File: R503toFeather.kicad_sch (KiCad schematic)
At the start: 4 parts, among them J1 MX1.0 6P

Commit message: RP2350 HSTX Production Version
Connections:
- net at A1.16 (SPARE): no longer J1.2 (GND)
- net at A1.17 (SDA): now also J1.2 (GND)

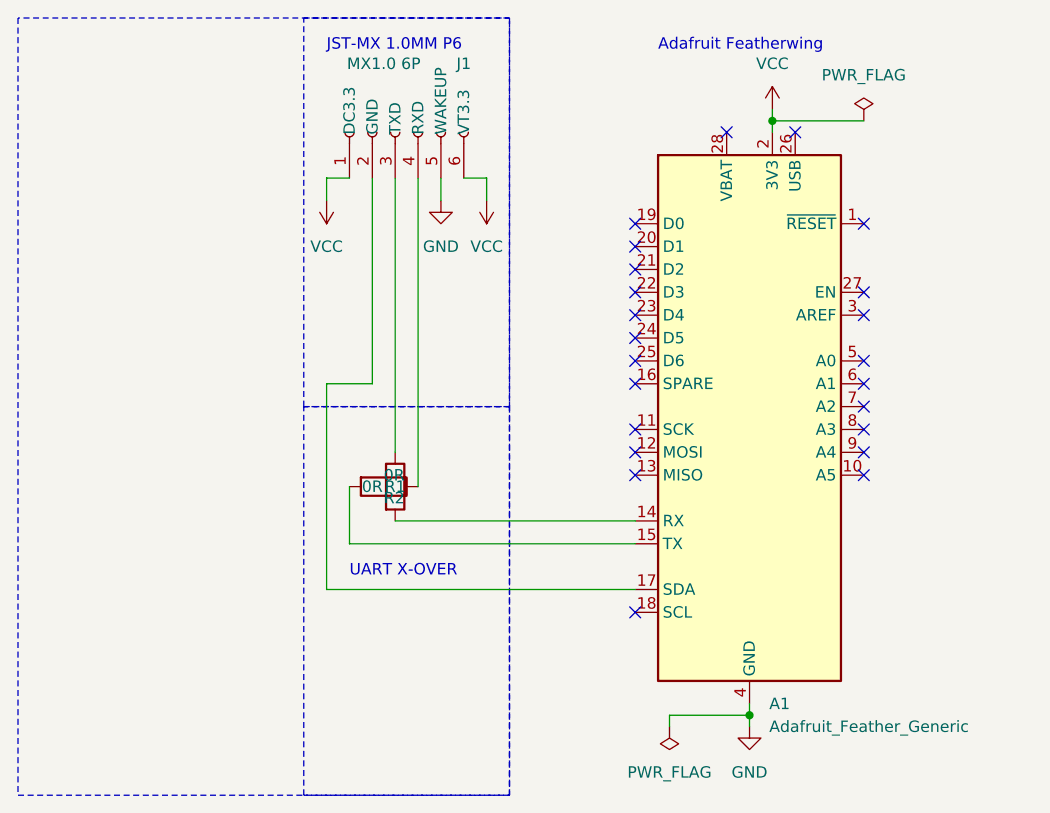
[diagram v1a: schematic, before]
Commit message: Fixed J1's 2 Pin. Corrected to GND.
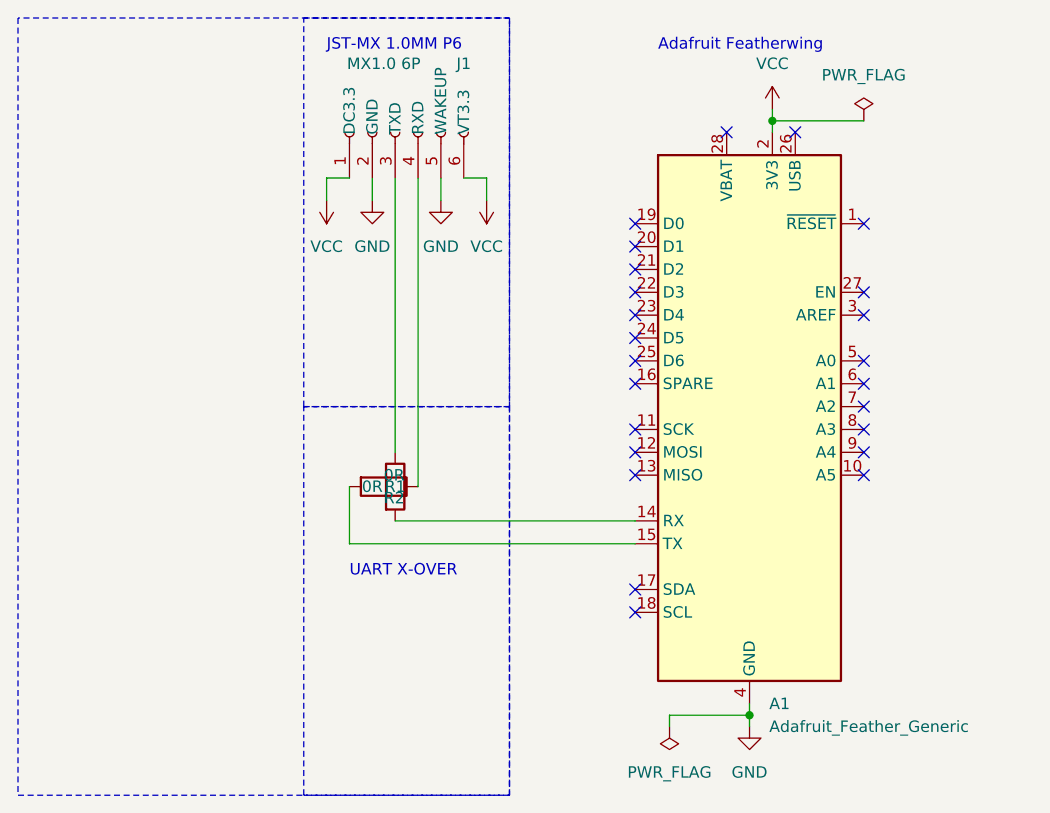
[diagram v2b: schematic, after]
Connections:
- net GND: now also J1.2 (GND)
- net at A1.17 (SDA): no longer J1.2 (GND)
- no-connect marks 23 -> 24
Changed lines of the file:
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@@
+	)
+	(no_connect
+		(at 138.43 130.81)
 	)
 	(no_connect
@@
 	(wire
 		(pts
-			(xy 104.14 107.95) (xy 104.14 130.81)
+			(xy 153.67 78.74) (xy 163.83 78.74)
+		)
+		(stroke
+			(width 0)
+			(type default)
+		)
+	)
+	(wire
+		(pts
+			(xy 151.13 144.78) (xy 151.13 146.05)
+		)
+		(stroke
+			(width 0)
+			(type default)
+		)
+	)
+	(wire
+		(pts
+			(xy 109.22 85.09) (xy 109.22 87.63)
 		)
 		(stroke
@@
 	(wire
 		(pts
-			(xy 104.14 130.81) (xy 138.43 130.81)
-		)
-		(stroke
-			(width 0)
-			(type default)
-			(color 0 0 255 1)
-		)
-	)
-	(wire
-		(pts
-			(xy 153.67 78.74) (xy 163.83 78.74)
-		)
-		(stroke
-			(width 0)
-			(type default)
-		)
-	)
-	(wire
-		(pts
-			(xy 151.13 144.78) (xy 151.13 146.05)
-		)
-		(stroke
-			(width 0)
-			(type default)
-		)
-	)
-	(wire
-		(pts
-			(xy 104.14 107.95) (xy 109.22 107.95)
-		)
-		(stroke
-			(width 0)
-			(type default)
-			(color 0 0 255 1)
-		)
-	)
-	(wire
-		(pts
 			(xy 116.84 85.09) (xy 116.84 87.63)
 		)
@@
 			(type default)
 			(color 0 0 0 1)
-		)
-	)
-	(wire
-		(pts
-			(xy 109.22 85.09) (xy 109.22 107.95)
-		)
-		(stroke
-			(width 0)
-			(type default)
-			(color 0 0 255 1)
 		)
 	)
@@
 					(unit 1)
 				)
+			)
+		)
+	)
+	(symbol
+		(lib_id "power:GND")
+		(at 109.22 87.63 0)
+		(unit 1)
+		(exclude_from_sim no)
+		(in_bom yes)
+		(on_board yes)
+		(dnp no)
+		(fields_autoplaced yes)
+		(property "Reference" "#PWR06"
+			(at 109.22 93.98 0)
+			(effects
+				(font
+					(size 1.27 1.27)
+				)
+				(hide yes)
+			)
+		)
+		(property "Value" "GND"
+			(at 109.22 92.71 0)
+			(effects
+				(font
+					(size 1.27 1.27)
+				)
+			)
+		)
+		(property "Footprint" ""
+			(at 109.22 87.63 0)
+			(effects
+				(font
+					(size 1.27 1.27)
+				)
+				(hide yes)
+			)
+		)
+		(property "Datasheet" ""
+			(at 109.22 87.63 0)
+			(effects
+				(font
+					(size 1.27 1.27)
+				)
+				(hide yes)
+			)
+		)
+		(property "Description" ""
+			(at 109.22 87.63 0)
+			(effects
+				(font
+					(size 1.27 1.27)
+				)
+			)
+		)
+		(pin "1"
+		)
+		(instances
+			(project "R503toFeather"
+				(path "/80f6c95f-f86e-4283-92dd-c1d765ce6a6d"
+					(reference "#PWR06")
+					(unit 1)
+				)
